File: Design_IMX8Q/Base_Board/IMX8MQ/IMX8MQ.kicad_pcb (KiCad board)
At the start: 8 copper layers, 50 x 80 mm, 97 parts, among them J1 Bus_PCI_Express_x16, Q1 AO3401A, U1 MIMX8MQ6CVAHZAB, U2 IS43LQ32256A-062BLI, U4 MP8759GD-Z, U5 MP2263GD-Z, U6 SDINBDG4-8G, U7 MT25QUxxxxxx1xW7, X1 ABLNO, Y1 27MHz, Y2 25MHz

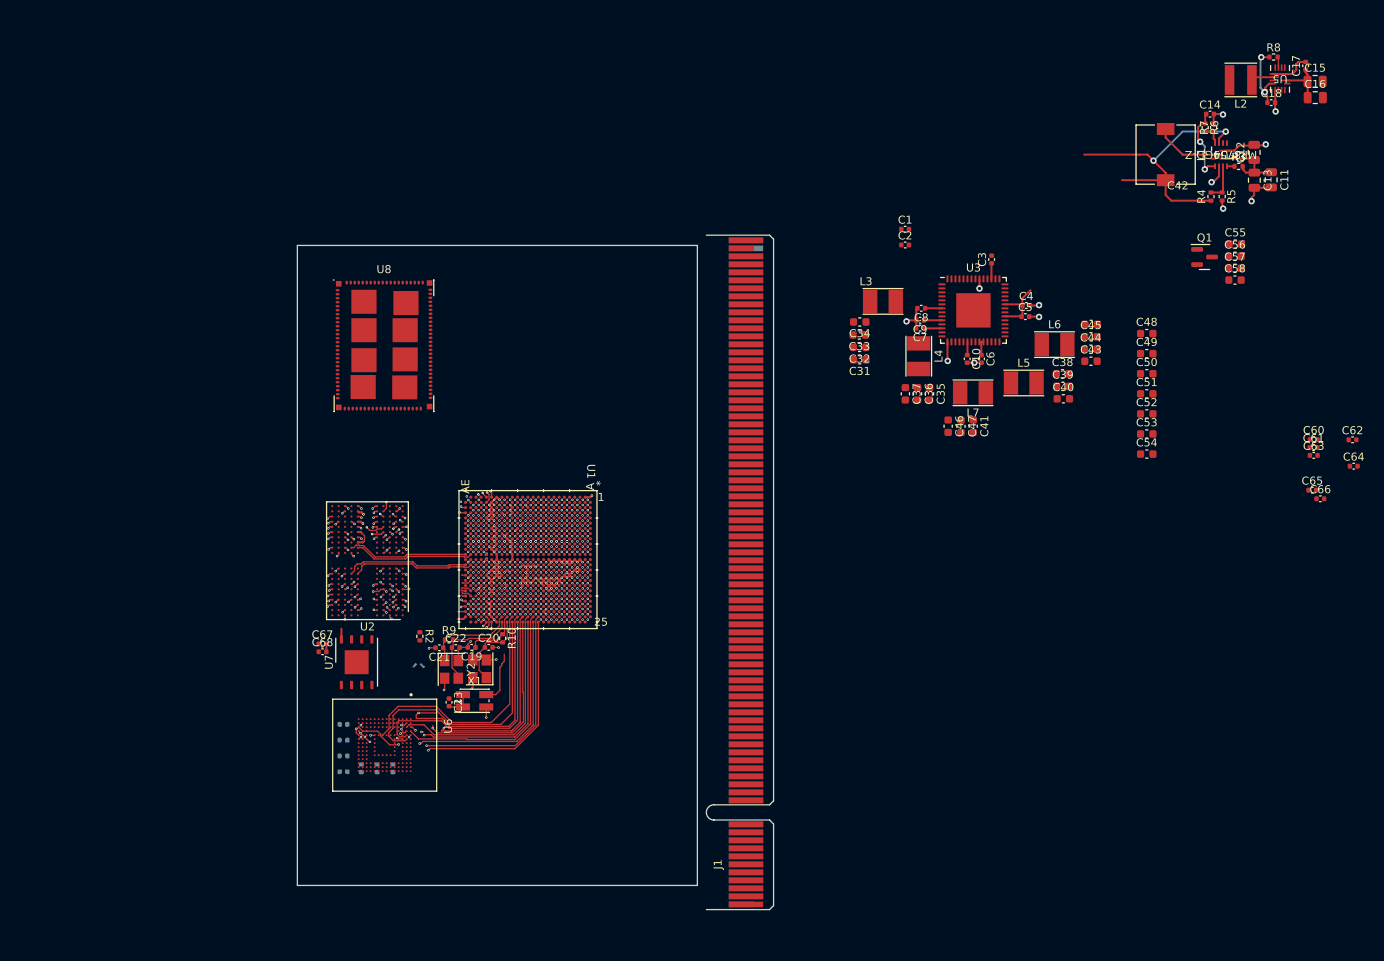
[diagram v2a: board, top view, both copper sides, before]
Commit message: changes vias pad size
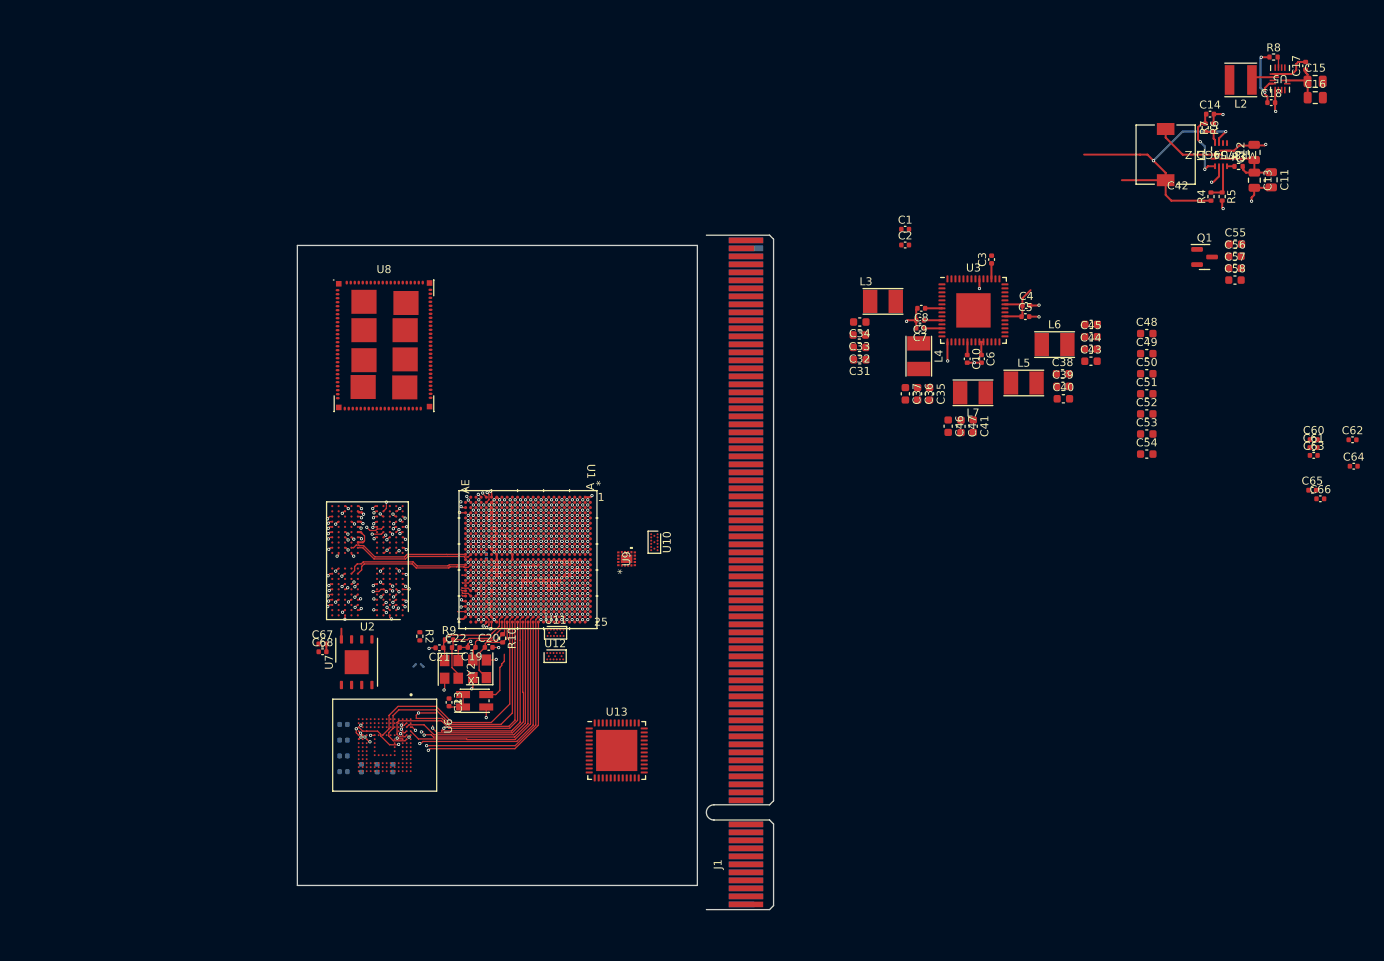
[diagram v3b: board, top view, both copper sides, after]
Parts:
- added U10: PCMF3USB3S, Package_CSP:Nexperia_WLCSP-15_6-3-6_2.37x1.17mm_Layout6x3_P0.4mm, F.Cu at (102.5, 80.7)
- added U11: PCMF3USB3S, Package_CSP:Nexperia_WLCSP-15_6-3-6_2.37x1.17mm_Layout6x3_P0.4mm, F.Cu at (90.2, 92.0)
- added U12: PCMF3USB3S, Package_CSP:Nexperia_WLCSP-15_6-3-6_2.37x1.17mm_Layout6x3_P0.4mm, F.Cu at (90.1, 95.0)
- added U13: KSZ9131RNXI, Package_DFN_QFN:VQFN-48-1EP_7x7mm_P0.5mm_EP5.15x5.15mm, F.Cu at (97.8, 106.8)
- added U9: PTN36043ABXY, _W_SBC:DHX2QFN18_SOT1442-1_NXP, F.Cu at (99.1, 82.8)
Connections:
- U1 pad A10: unconnected-(U1F-USB2_DP-PadA10) -> Net-(U12A-CH1_OUT+)
- U1 pad A11: unconnected-(U1E-USB1_RESREF-PadA11) -> USB1_RESREF
- U1 pad A12: unconnected-(U1E-USB1_RX_P-PadA12) -> USB1_RX_P
- U1 pad A13: unconnected-(U1E-USB1_TX_P-PadA13) -> USB1_TX_P
- U1 pad A14: unconnected-(U1E-USB1_DP-PadA14) -> USB1_DP
- U1 pad A6: unconnected-(U1E-UART3_RXD-PadA6) -> WIFI/BLE_TX
- U1 pad A8: unconnected-(U1F-USB2_RX_P-PadA8) -> Net-(U11C-CH3_OUT+)
- U1 pad A9: unconnected-(U1F-USB2_TX_P-PadA9) -> Net-(U11C-CH3_OUT-)
- U1 pad B10: unconnected-(U1F-USB2_DN-PadB10) -> Net-(U12A-CH1_OUT-)
- U1 pad B12: unconnected-(U1E-USB1_RX_N-PadB12) -> USB1_RX_N
- U1 pad B13: unconnected-(U1E-USB1_TX_N-PadB13) -> USB1_TX_N
- U1 pad B14: unconnected-(U1E-USB1_DN-PadB14) -> USB1_DN
- U1 pad B4: unconnected-(U1B-ECSPI1_MISO-PadB4) -> WIFI/BLE_RTS
- U1 pad B7: unconnected-(U1E-UART3_TXD-PadB7) -> WIFI/BLE_RX
- U1 pad B8: unconnected-(U1F-USB2_RX_N-PadB8) -> Net-(U12B-CH2_OUT+)
- U1 pad B9: unconnected-(U1F-USB2_TX_N-PadB9) -> Net-(U12B-CH2_OUT-)
- U1 pad C14: unconnected-(U1E-USB1_ID-PadC14) -> USB1_ID
- U1 pad D14: unconnected-(U1E-USB1_VBUS-PadD14) -> USB1_VBUS
- U1 pad D4: unconnected-(U1B-ECSPI1_SS0-PadD4) -> WIFI/BLE_CTS
- U1 pad G5: unconnected-(U1E-SAI2_TXD0-PadG5) -> WIFI/BLE_SDIO_PCMIN
- U1 pad H6: unconnected-(U1E-SAI2_RXD0-PadH6) -> WIFI/BLE_SDIO_PCMOUT
- U1 pad J4: unconnected-(U1E-SAI2_RXFS-PadJ4) -> WIFI/BLE_PCMRF1
- U1 pad J5: unconnected-(U1E-SAI2_TXC-PadJ5) -> WIFI/BLE_SDIO_PCMCLK
- U1 pad L22: unconnected-(U1E-SD2_CLK-PadL22) -> WIFI/BLE_SDIO_CLK
- U1 pad M21: unconnected-(U1E-SD2_WP-PadM21) -> WIFI/BLE_SDIO_STROBE
- U1 pad M22: unconnected-(U1E-SD2_CMD-PadM22) -> WIFI/BLE_SDIO_CMD
- U1 pad N19: unconnected-(U1B-ENET_MDIO-PadN19) -> ENET_MDIO
- U1 pad N20: unconnected-(U1B-ENET_MDC-PadN20) -> ENET_MDC
- U1 pad N21: unconnected-(U1E-SD2_DATA1-PadN21) -> WIFI/BLE_SDIO_DATA1
- U1 pad N22: unconnected-(U1E-SD2_DATA0-PadN22) -> WIFI/BLE_SDIO_DATA0
- U1 pad P19: unconnected-(U1B-ENET_TX_CTL-PadP19) -> ENET_TX_CL
- U1 pad P20: unconnected-(U1B-ENET_TD3-PadP20) -> ENET_TD3
- U1 pad P21: unconnected-(U1E-SD2_DATA3-PadP21) -> WIFI/BLE_SDIO_DATA3
- U1 pad P22: unconnected-(U1E-SD2_DATA2-PadP22) -> WIFI/BLE_SDIO_DATA2
- U1 pad R16: VDD_SOC -> GND
- U1 pad R17: unconnected-(U1G-EFUSE_VQPS-PadR17) -> GND
- U1 pad R19: unconnected-(U1C-ENET_TD2-PadR19) -> ENET_TD2
- U1 pad R20: unconnected-(U1C-ENET_TD0-PadR20) -> ENET_TD0
- U1 pad R21: unconnected-(U1C-ENET_TD1-PadR21) -> ENET_TD1
- U1 pad R22: unconnected-(U1E-SD2_RESET_B-PadR22) -> WIFI/BLE_SDIO_nRST
- U1 pad T16: unconnected-(U1I-VDDA_1P8_TSENSOR-PadT16) -> GND
- U1 pad T17: VDD_SOC -> GND
- U1 pad T19: unconnected-(U1B-ENET_TXC-PadT19) -> ENET_TXC
- U1 pad T20: unconnected-(U1B-ENET_RXC-PadT20) -> ENET_RXC
- U1 pad T21: unconnected-(U1C-ENET_RX_CTL-PadT21) -> ENET_RX_CTL
- U1 pad U19: unconnected-(U1C-ENET_RD0-PadU19) -> ENET_RD0
- U1 pad U20: unconnected-(U1C-ENET_RD2-PadU20) -> ENET_RD2
- U1 pad U21: unconnected-(U1C-ENET_RD1-PadU21) -> ENET_RD1
- U1 pad V19: unconnected-(U1C-ENET_RD3-PadV19) -> ENET_RD3
- U8 pad 100: Net-(U8B-GND-Pad100) -> GND
- U8 pad 101: Net-(U8B-GND-Pad100) -> GND
- U8 pad 102: Net-(U8B-GND-Pad100) -> GND
- U8 pad 103: Net-(U8B-GND-Pad100) -> GND
- U8 pad 105: Net-(U8B-GND-Pad100) -> GND
- U8 pad 106: Net-(U8B-GND-Pad100) -> GND
- U8 pad 107: Net-(U8B-GND-Pad100) -> GND
- U8 pad 108: Net-(U8B-GND-Pad100) -> GND
- U8 pad 17: unconnected-(U8B-GND-Pad17) -> GND
- U8 pad 20: unconnected-(U8B-GND-Pad20) -> GND
- U8 pad 23: unconnected-(U8B-GND-Pad23) -> GND
- U8 pad 26: unconnected-(U8B-GND-Pad26) -> GND
- U8 pad 32: unconnected-(U8B-GND-Pad32) -> GND
- U8 pad 35: unconnected-(U8B-GND-Pad35) -> GND
- U8 pad 38: unconnected-(U8B-GND-Pad38) -> GND
- U8 pad 4: unconnected-(U8B-VDD-Pad4) -> Net-(U8B-VDD-Pad4)
- U8 pad 41: unconnected-(U8B-GND-Pad41) -> GND
- U8 pad 45: unconnected-(U8A-SDIO_RESET#-Pad45) -> WIFI/BLE_SDIO_nRST
- U8 pad 46: unconnected-(U8A-SDIO_WAKE#-Pad46) -> WIFI/BLE_SDIO_STROBE
- U8 pad 47: unconnected-(U8A-SDIO_DATA3-Pad47) -> WIFI/BLE_SDIO_DATA3
- U8 pad 48: unconnected-(U8A-SDIO_DATA2-Pad48) -> WIFI/BLE_SDIO_DATA2
- U8 pad 49: unconnected-(U8A-SDIO_DATA1-Pad49) -> WIFI/BLE_SDIO_DATA1
- U8 pad 50: unconnected-(U8A-SDIO_DATA0-Pad50) -> WIFI/BLE_SDIO_DATA0
- U8 pad 51: unconnected-(U8A-SDIO_CMD-Pad51) -> WIFI/BLE_SDIO_CMD
- U8 pad 52: unconnected-(U8A-SDIO_CLK-Pad52) -> WIFI/BLE_SDIO_CLK
- U8 pad 54: unconnected-(U8A-UART_CTS-Pad54) -> WIFI/BLE_CTS
- U8 pad 55: unconnected-(U8A-UART_TX-Pad55) -> WIFI/BLE_TX
- U8 pad 56: unconnected-(U8A-UART_RX-Pad56) -> WIFI/BLE_RX
- U8 pad 57: unconnected-(U8A-UART_RTS-Pad57) -> WIFI/BLE_RTS
- U8 pad 58: unconnected-(U8A-PCMRF1-Pad58) -> WIFI/BLE_PCMRF1
- U8 pad 59: unconnected-(U8A-PCMIN-Pad59) -> WIFI/BLE_SDIO_PCMIN
- U8 pad 6: unconnected-(U8B-GND-Pad6) -> GND
- U8 pad 60: unconnected-(U8A-PCMOUT-Pad60) -> WIFI/BLE_SDIO_PCMOUT
- U8 pad 61: unconnected-(U8A-PCMCLK-Pad61) -> WIFI/BLE_SDIO_PCMCLK
- U8 pad 62: unconnected-(U8B-GND-Pad62) -> GND
- U8 pad 63: unconnected-(U8A-BT_EN-Pad63) -> WIFI/BLE_SDIO_BT_EN
- U8 pad 68: unconnected-(U8B-GND-Pad68) -> GND
- U8 pad 71: unconnected-(U8B-GND-Pad71) -> GND
- U8 pad 72: unconnected-(U8B-VDD-Pad72) -> Net-(U8B-VDD-Pad4)
- U8 pad 73: unconnected-(U8B-VDD-Pad73) -> Net-(U8B-VDD-Pad4)
- U8 pad 75: Net-(U8B-GND-Pad100) -> GND
- U8 pad 76: Net-(U8B-GND-Pad100) -> GND
- U8 pad 77: Net-(U8B-GND-Pad100) -> GND
- U8 pad 78: Net-(U8B-GND-Pad100) -> GND
- U8 pad 79: Net-(U8B-GND-Pad100) -> GND
- U8 pad 80: Net-(U8B-GND-Pad100) -> GND
- U8 pad 81: Net-(U8B-GND-Pad100) -> GND
- U8 pad 82: Net-(U8B-GND-Pad100) -> GND
- U8 pad 83: Net-(U8B-GND-Pad100) -> GND
- U8 pad 84: Net-(U8B-GND-Pad100) -> GND
- U8 pad 85: Net-(U8B-GND-Pad100) -> GND
- U8 pad 86: Net-(U8B-GND-Pad100) -> GND
- U8 pad 87: Net-(U8B-GND-Pad100) -> GND
- U8 pad 88: Net-(U8B-GND-Pad100) -> GND
- U8 pad 89: Net-(U8B-GND-Pad100) -> GND
- U8 pad 90: Net-(U8B-GND-Pad100) -> GND
- U8 pad 91: Net-(U8B-GND-Pad100) -> GND
- U8 pad 92: Net-(U8B-GND-Pad100) -> GND
- U8 pad 93: Net-(U8B-GND-Pad100) -> GND
- U8 pad 94: Net-(U8B-GND-Pad100) -> GND
- U8 pad 95: Net-(U8B-GND-Pad100) -> GND
- U8 pad 96: Net-(U8B-GND-Pad100) -> GND
- U8 pad 97: Net-(U8B-GND-Pad100) -> GND
- U8 pad 98: Net-(U8B-GND-Pad100) -> GND
- U8 pad 99: Net-(U8B-GND-Pad100) -> GND
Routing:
- net GND: vias 587 -> 599
- net DRAM_DATA11_A: vias 13 -> 1

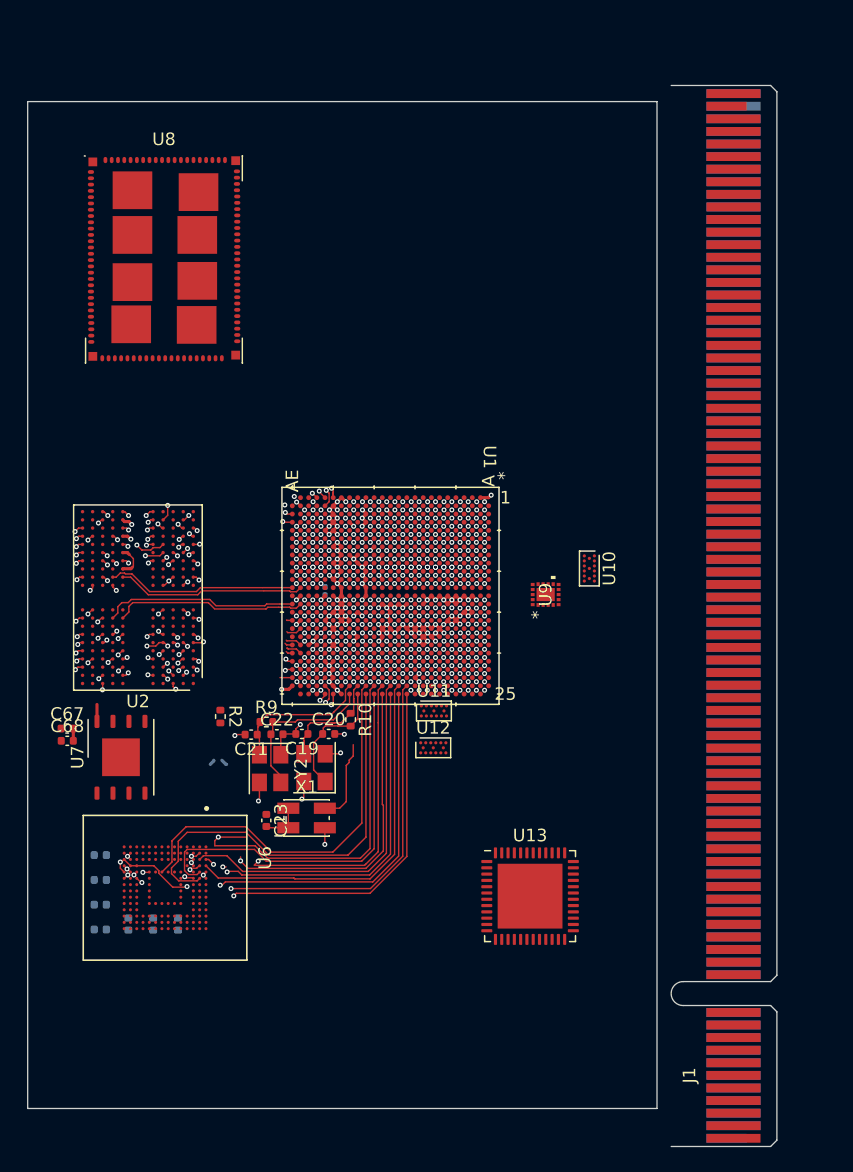
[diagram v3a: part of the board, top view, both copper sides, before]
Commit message: Update IMX6QP and IMX8MQ
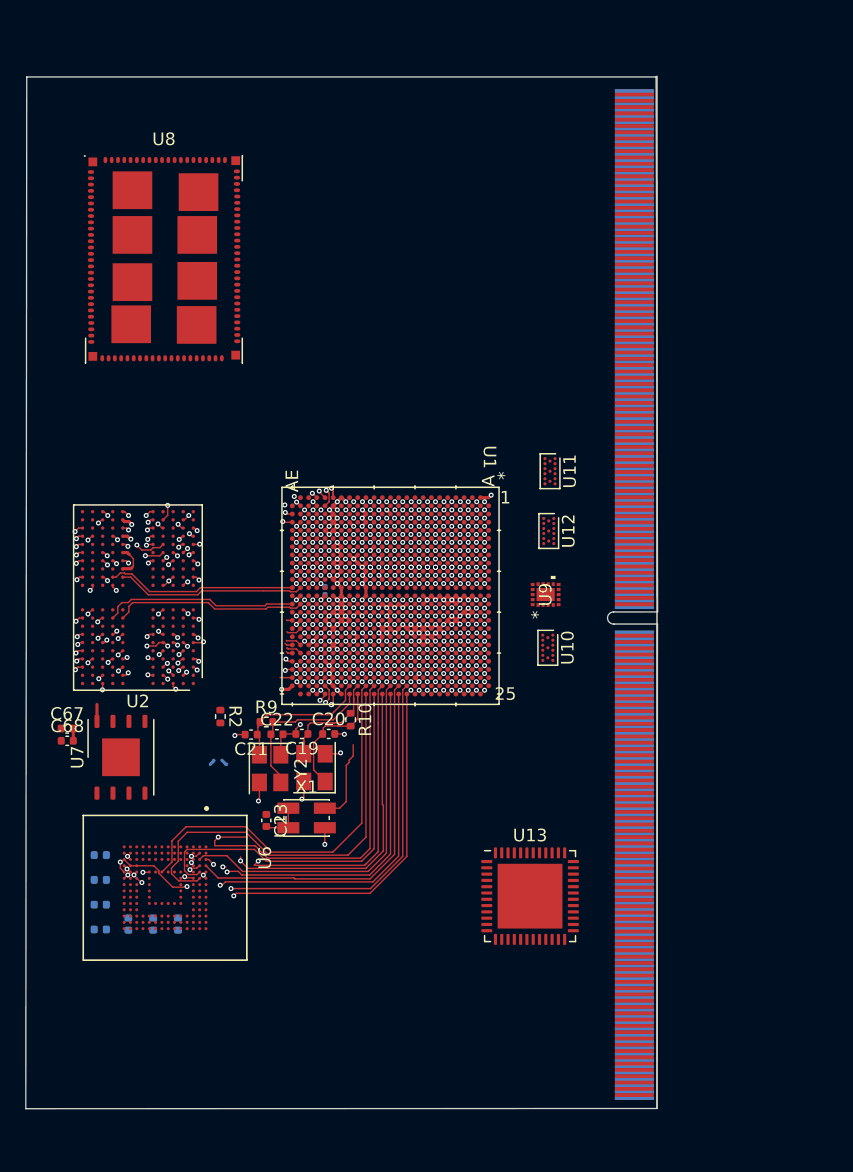
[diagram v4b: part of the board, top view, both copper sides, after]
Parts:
- removed J1: Bus_PCI_Express_x16, Connector_PCBEdge:BUS_PCIexpress_x16
- added U14: IMX6ModuleConector_300, _W_SBC:IMX6QPModule_R300, F.Cu at (103.1, 84.8)
- moved U11 21.2 mm to (99.4, 73.0), turned to -90 degrees
- moved U12 19.5 mm to (99.3, 77.8), turned to -90 degrees
- moved U10 7.11 mm to (99.2, 87.0)
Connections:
- U1 pad A15: unconnected-(U1D-MIPI_DSI_D3_N-PadA15) -> MIPI_DSI_D3_-
- U1 pad A16: unconnected-(U1D-MIPI_DSI_D1_N-PadA16) -> MIPI_DSI_D1_-
- U1 pad A17: unconnected-(U1D-MIPI_DSI_D0_N-PadA17) -> MIPI_DSI_D0_-
- U1 pad A18: unconnected-(U1D-MIPI_DSI_D2_N-PadA18) -> MIPI_DSI_D2_-
- U1 pad A19: unconnected-(U1C-MIPI_CSI2_CLK_N-PadA19) -> MIPI_CSI2_CLK-
- U1 pad A20: unconnected-(U1D-MIPI_CSI2_D1_N-PadA20) -> MIPI_CSI2_D1_-
- U1 pad A21: unconnected-(U1D-MIPI_CSI2_D2_N-PadA21) -> MIPI_CSI2_D2_-
- U1 pad A22: unconnected-(U1C-MIPI_CSI1_CLK_N-PadA22) -> MIPI_CSI1_CLK-
- U1 pad A23: unconnected-(U1D-MIPI_CSI1_D0_N-PadA23) -> MIPI_CSI1_D0_-
- U1 pad B15: unconnected-(U1D-MIPI_DSI_D3_P-PadB15) -> MIPI_DSI_D3_+
- U1 pad B16: unconnected-(U1D-MIPI_DSI_D1_P-PadB16) -> MIPI_DSI_D1_+
- U1 pad B17: unconnected-(U1D-MIPI_DSI_D0_P-PadB17) -> MIPI_DSI_D0_+
- U1 pad B18: unconnected-(U1D-MIPI_DSI_D2_P-PadB18) -> MIPI_DSI_D2_+
- U1 pad B19: unconnected-(U1C-MIPI_CSI2_CLK_P-PadB19) -> MIPI_CSI2_CLK+
- U1 pad B20: unconnected-(U1D-MIPI_CSI2_D1_P-PadB20) -> MIPI_CSI2_D1_+
- U1 pad B21: unconnected-(U1D-MIPI_CSI2_D2_P-PadB21) -> MIPI_CSI2_D2_+
- U1 pad B22: unconnected-(U1C-MIPI_CSI1_CLK_P-PadB22) -> MIPI_CSI1_CLK+
- U1 pad B23: unconnected-(U1D-MIPI_CSI1_D0_P-PadB23) -> MIPI_CSI1_D0_+
- U1 pad B24: unconnected-(U1D-MIPI_CSI1_D2_N-PadB24) -> MIPI_CSI1_D2_-
- U1 pad C16: unconnected-(U1C-MIPI_DSI_CLK_N-PadC16) -> MIPI_DSI_CLK-
- U1 pad C17: unconnected-(U1C-MIPI_DSI_REXT-PadC17) -> MIPI_DSI_REXT
- U1 pad C19: unconnected-(U1D-MIPI_CSI2_D3_N-PadC19) -> MIPI_CSI2_D3_-
- U1 pad C20: unconnected-(U1D-MIPI_CSI2_D0_N-PadC20) -> MIPI_CSI2_D0_-
- U1 pad C21: unconnected-(U1D-MIPI_CSI1_D3_N-PadC21) -> MIPI_CSI1_D3_-
- U1 pad C22: unconnected-(U1D-MIPI_CSI1_D1_N-PadC22) -> MIPI_CSI1_D1_-
- U1 pad C23: unconnected-(U1D-MIPI_CSI1_D2_P-PadC23) -> MIPI_CSI1_D2_+
- U1 pad C25: unconnected-(U1D-PCIE2_RESREF-PadC25) -> PCIE2_RESREF
- U1 pad D16: unconnected-(U1C-MIPI_DSI_CLK_P-PadD16) -> MIPI_DSI_CLK+
- U1 pad D19: unconnected-(U1D-MIPI_CSI2_D3_P-PadD19) -> MIPI_CSI2_D3_+
- U1 pad D20: unconnected-(U1D-MIPI_CSI2_D0_P-PadD20) -> MIPI_CSI2_D0_+
- U1 pad D21: unconnected-(U1D-MIPI_CSI1_D3_P-PadD21) -> MIPI_CSI1_D3_+
- U1 pad D22: unconnected-(U1D-MIPI_CSI1_D1_P-PadD22) -> MIPI_CSI1_D1_+
- U1 pad D24: unconnected-(U1D-PCIE2_RXN_N-PadD24) -> PCIE2_RXN_-
- U1 pad D25: unconnected-(U1D-PCIE2_RXN_P-PadD25) -> PCIE2_RXN_+
- U1 pad E24: unconnected-(U1D-PCIE2_TXN_N-PadE24) -> PCIE2_TXN_-
- U1 pad E25: unconnected-(U1D-PCIE2_TXN_P-PadE25) -> PCIE2_TXN_+
- U1 pad F24: unconnected-(U1D-PCIE2_REF_PAD_C_LK_N-PadF24) -> PCIE2_REF_PAD_CLK_-
- U1 pad F25: unconnected-(U1D-PCIE2_REF_PAD_C_LK_P-PadF25) -> PCIE2_REF_PAD_CLK_+
- U1 pad G25: unconnected-(U1D-PCIE1_RESREF-PadG25) -> PCIE1_RESREF
- U1 pad H24: unconnected-(U1D-PCIE1_RXN_N-PadH24) -> PCIE1_RXN_-
- U1 pad H25: unconnected-(U1D-PCIE1_RXN_P-PadH25) -> PCIE1_RXN_+
- U1 pad J24: unconnected-(U1D-PCIE1_TXN_N-PadJ24) -> PCIE1_TXN_-
- U1 pad J25: unconnected-(U1D-PCIE1_TXN_P-PadJ25) -> PCIE1_TXN_+
- U1 pad K24: unconnected-(U1D-PCIE1_REF_PAD_C_LK_N-PadK24) -> PCIE1_REF_PAD_CLK_-
- U1 pad K25: unconnected-(U1D-PCIE1_REF_PAD_C_LK_P-PadK25) -> PCIE1_REF_PAD_CLK_+
- U1 pad M1: unconnected-(U1C-HDMI_TX_P_LN_3-PadM1) -> HDMI_TX_LN_3_+
- U1 pad M2: unconnected-(U1C-HDMI_TX_M_LN_3-PadM2) -> HDMI_TX_LN_3_-
- U1 pad N1: unconnected-(U1C-HDMI_TX_M_LN_2-PadN1) -> HDMI_TX_LN_2_-
- U1 pad N2: unconnected-(U1C-HDMI_TX_P_LN_2-PadN2) -> HDMI_TX_LN_2_+
- U1 pad P1: unconnected-(U1C-HDMI_REXT-PadP1) -> HDMI_REXT
- U1 pad P3: unconnected-(U1C-HDMI_DDC_SDA-PadP3) -> HDMI_DDC_SDA
- U1 pad R1: unconnected-(U1C-HDMI_REFCLK_N-PadR1) -> HDMI_REFCLK_-
- U1 pad R16: GND -> VDD_SOC
- U1 pad R17: GND -> unconnected-(U1G-EFUSE_VQPS-PadR17)
- U1 pad R2: unconnected-(U1C-HDMI_REFCLK_P-PadR2) -> HDMI_REFCLK_+
- U1 pad R3: unconnected-(U1C-HDMI_DDC_SCL-PadR3) -> HDMI_DDC_SCL
- U1 pad T1: unconnected-(U1C-HDMI_TX_P_LN_0-PadT1) -> HDMI_TX_LN_0_+
- U1 pad T16: GND -> unconnected-(U1I-VDDA_1P8_TSENSOR-PadT16)
- U1 pad T17: GND -> VDD_SOC
- U1 pad T2: unconnected-(U1C-HDMI_TX_M_LN_0-PadT2) -> HDMI_TX_LN_0_-
- U1 pad T5: unconnected-(U1C-JTAG_TCK-PadT5) -> JTAG_TCK
- U1 pad U1: unconnected-(U1C-HDMI_TX_M_LN_1-PadU1) -> HDMI_TX_LN_1_-
- U1 pad U2: unconnected-(U1C-HDMI_TX_P_LN_1-PadU2) -> HDMI_TX_LN_1_+
- U1 pad U5: unconnected-(U1C-JTAG_TDO-PadU5) -> JTAG_TDO
- U1 pad U6: unconnected-(U1C-JTAG_TRST_B-PadU6) -> JTAG_TRST_B
- U1 pad U7: unconnected-(U1C-JTAG_MOD-PadU7) -> JTAG_MOD
- U1 pad V1: unconnected-(U1C-HDMI_AUX_P-PadV1) -> HDMI_AUX_+
- U1 pad V2: unconnected-(U1C-HDMI_AUX_N-PadV2) -> HDMI_AUX_-
- U1 pad V5: unconnected-(U1C-JTAG_TMS-PadV5) -> JTAG_TMS
- U1 pad W2: unconnected-(U1C-HDMI_HPD-PadW2) -> HDMI_HPD
- U1 pad W3: unconnected-(U1C-HDMI_CEC-PadW3) -> HDMI_CEC
- U1 pad W5: unconnected-(U1C-JTAG_TDI-PadW5) -> JTAG_TDI
- U13 pad 24: unconnected-(U13-TXC-Pad24) -> ENET_TXC
- U13 pad 25: unconnected-(U13-TX_CTL-Pad25) -> ENET_TX_CL
- U13 pad 33: unconnected-(U13-RX_CTL/CLK125_EN-Pad33) -> ENET_RX_CTL
- U13 pad 35: unconnected-(U13-RXC/PHYAD2-Pad35) -> ENET_RXC
- U13 pad 36: unconnected-(U13-MDC-Pad36) -> ENET_MDC
- U13 pad 37: unconnected-(U13-MDIO-Pad37) -> ENET_MDIO
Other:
- board size 50 x 80 mm -> 50.2 x 82 mm
